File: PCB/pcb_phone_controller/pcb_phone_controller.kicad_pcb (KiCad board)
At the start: 2 copper layers, 115.3 x 53.2 mm, 39 parts, among them SW17 SS-12D00-G 4 E, X1 KAILH-MINI-SILENT-SWITCH, Y1 KAILH-MINI-SILENT-SWITCH

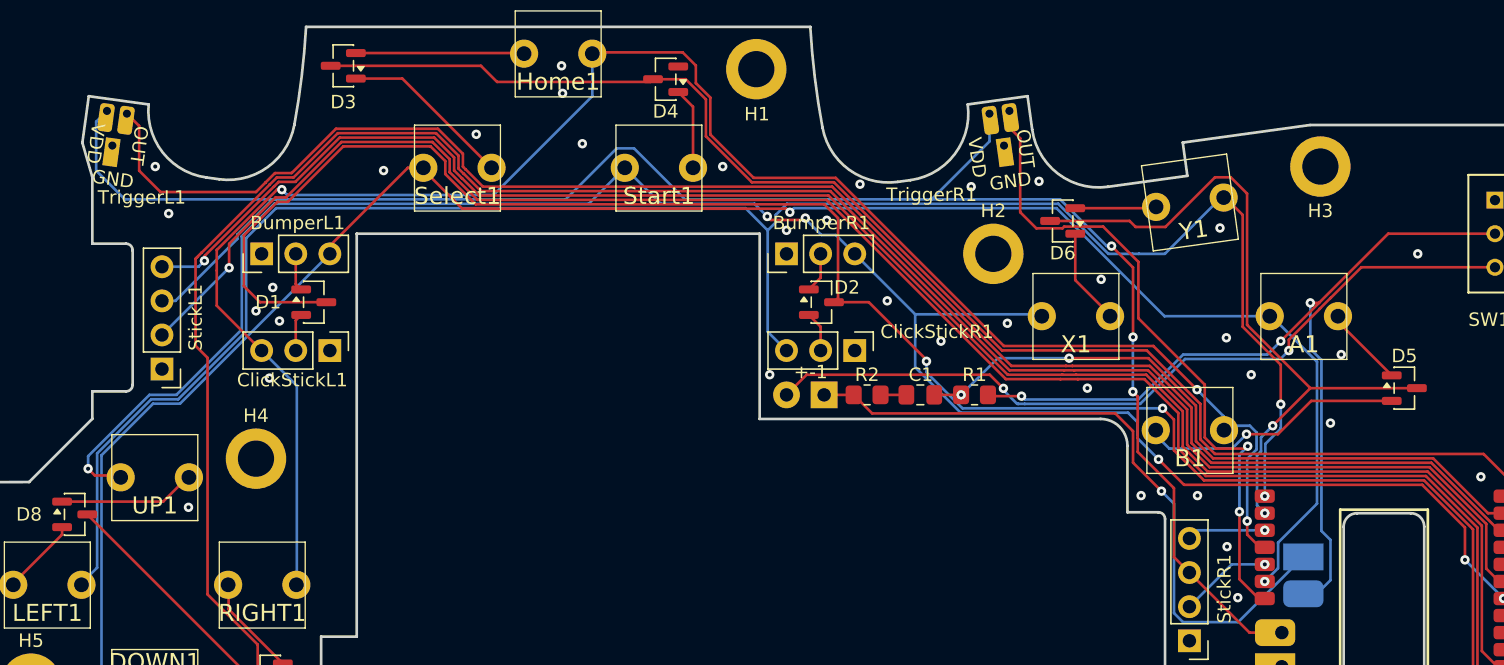
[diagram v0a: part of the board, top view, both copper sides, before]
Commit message: Change capacitives buttons to digitals ones and add real pullup
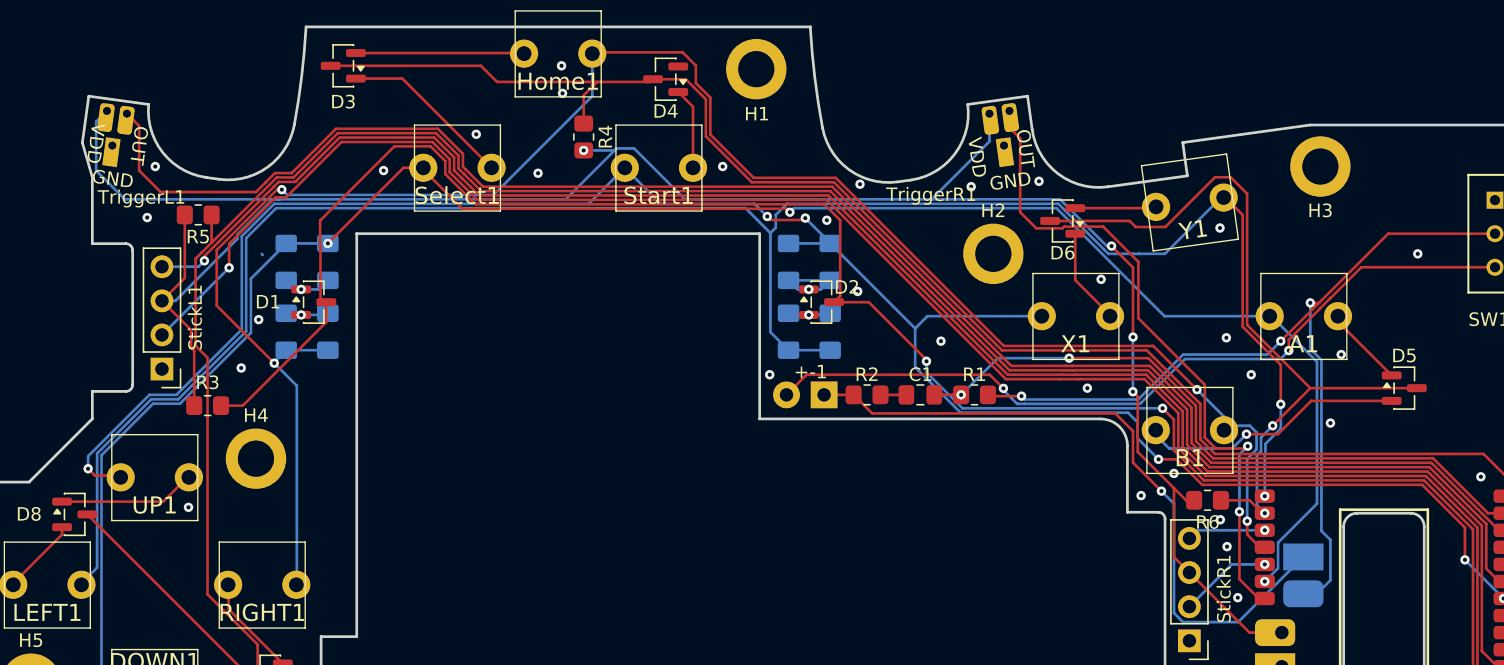
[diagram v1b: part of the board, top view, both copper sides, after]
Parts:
- added R3: 10k, Resistor_SMD:R_0805_2012Metric_Pad1.20x1.40mm_HandSolder, F.Cu at (123.9, 123.3)
- added R4: 10k, Resistor_SMD:R_0805_2012Metric_Pad1.20x1.40mm_HandSolder, F.Cu at (151.9, 103.3)
- added R5: 10k, Resistor_SMD:R_0805_2012Metric_Pad1.20x1.40mm_HandSolder, F.Cu at (123.2, 109.1)
- added R6: 10k, Resistor_SMD:R_0805_2012Metric_Pad1.20x1.40mm_HandSolder, F.Cu at (198.3, 130.3)
- BumperL1, BumperR1, ClickStickL1, ClickStickR1: value ~ -> Thin membrane button; footprint Lib_controller:TTP223 -> Lib_controller:SKRWADE030; moved to B.Cu
- moved ClickStickR1 3.66 mm to (168.7, 117.8), turned to 180 degrees
- moved BumperL1 3.43 mm to (131.3, 112.6), turned to 180 degrees
- moved ClickStickL1 2.20 mm to (131.3, 117.8), turned to 180 degrees
- moved BumperR1 1.80 mm to (168.7, 112.6), turned to 180 degrees
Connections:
- BumperL1 pad 1: GND -> Column 0
- BumperR1 pad 1: GND -> Column 2
- ClickStickL1 pad 1: GND -> Net-(ClickStickL1-Pad1)
- ClickStickL1 pad 2: Net-(ClickStickL1-I/O) -> Column 1
- ClickStickR1 pad 1: GND -> Net-(ClickStickR1-Pad1)
- ClickStickR1 pad 2: Net-(ClickStickR1-I/O) -> Column 3
- D1 pad 2: Net-(ClickStickL1-I/O) -> Net-(ClickStickL1-Pad1)
- D2 pad 2: Net-(ClickStickR1-I/O) -> Net-(ClickStickR1-Pad1)
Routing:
- net +3.3V: track 141.5 -> 161.8 mm, vias 3 -> 4
- net Column 1: track 137.4 -> 141.9 mm, vias 3 -> 4
- net Net-(BumperR1-Pad2): track 3.01 -> 6.76 mm, vias 0 -> 1
- net Row 2: track 52.5 -> 56.1 mm
- net Column 2: track 149.4 -> 153.1 mm
- net Row 1: track 114.9 -> 118.5 mm
- net Column 3: track 145.0 -> 148.2 mm
- net Net-(ClickStickR1-Pad1): track 0.00 -> 3.20 mm, vias 0 -> 1
- net Net-(ClickStickL1-Pad1): track 0.00 -> 3.20 mm, vias 0 -> 1
- net Net-(ClickStickR1-I/O): track 3.01 -> 0.00 mm
- net Net-(ClickStickL1-I/O): track 2.82 -> 0.00 mm
- net Column 0: track 142.2 -> 144.3 mm, vias 2 -> 3
- net Row 3: track 169.8 -> 171.9 mm
- net Row 0: track 144.4 -> 146.4 mm
- net Net-(BumperL1-Pad2): track 2.82 -> 3.66 mm, vias 0 -> 1
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
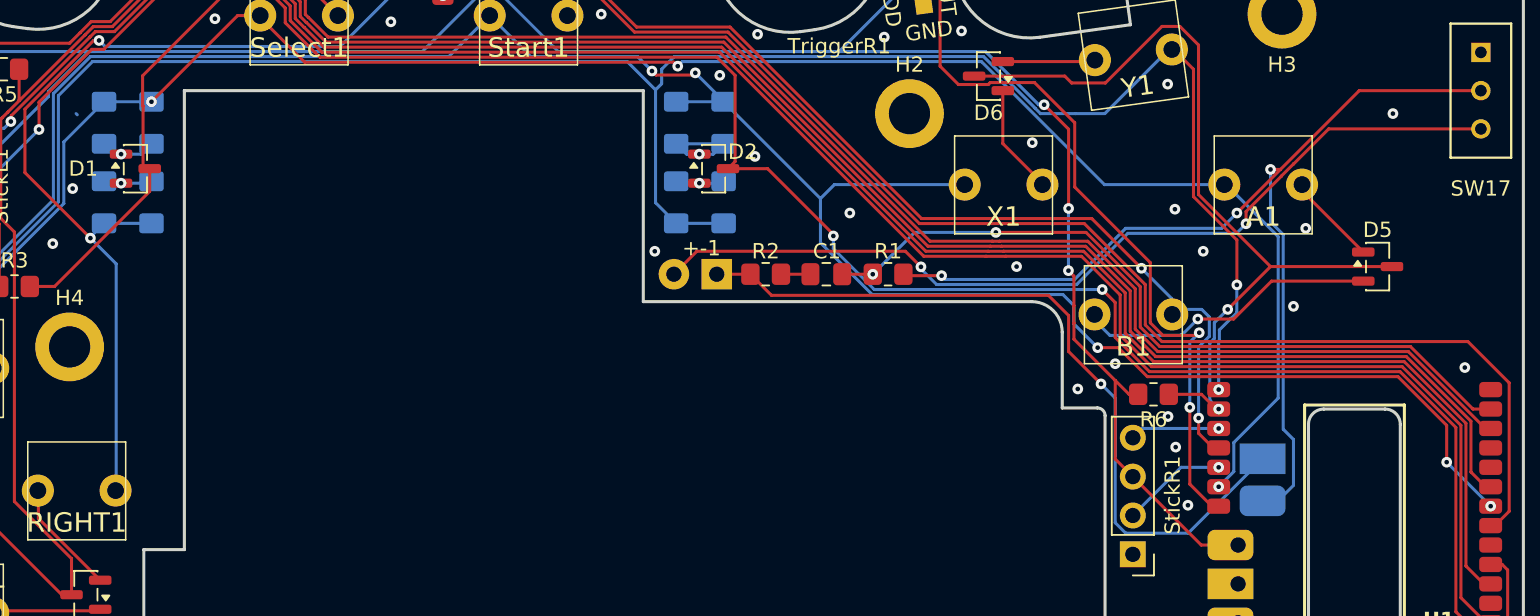
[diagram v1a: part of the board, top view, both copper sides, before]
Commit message: Add a 3D model for the back buttons
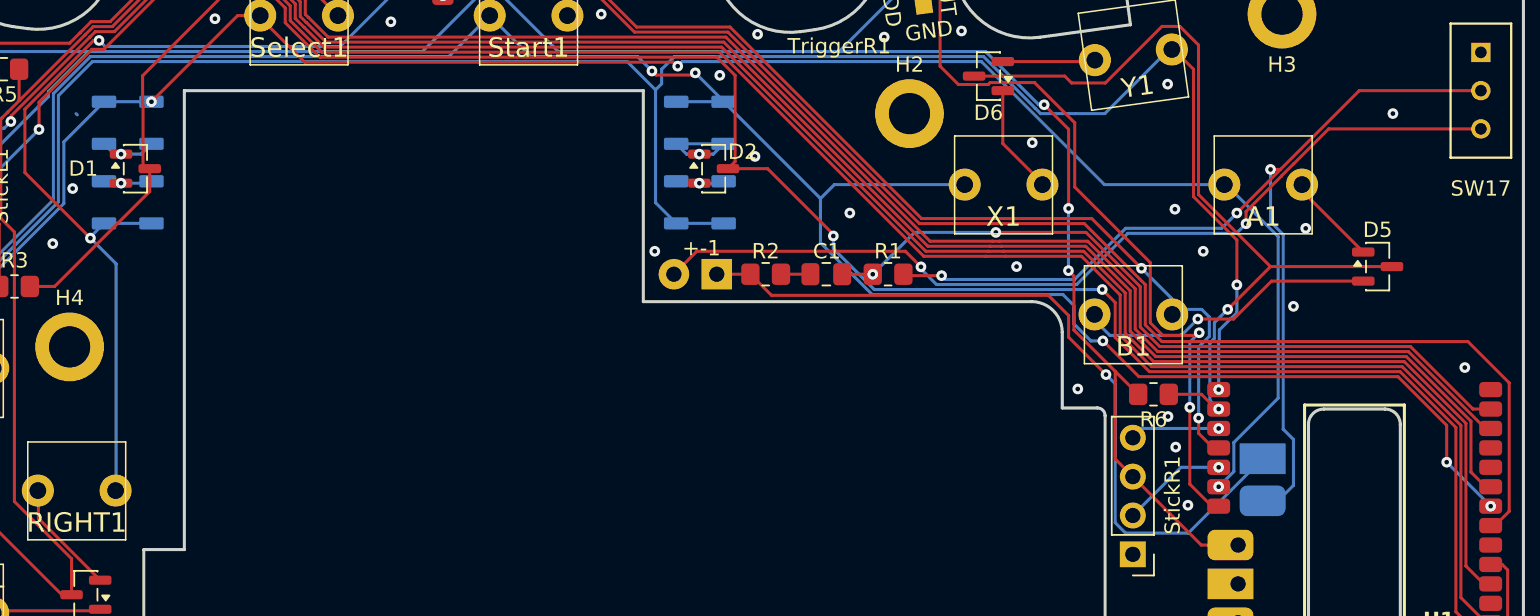
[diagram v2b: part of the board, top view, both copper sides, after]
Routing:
- net GND: vias 32 -> 31

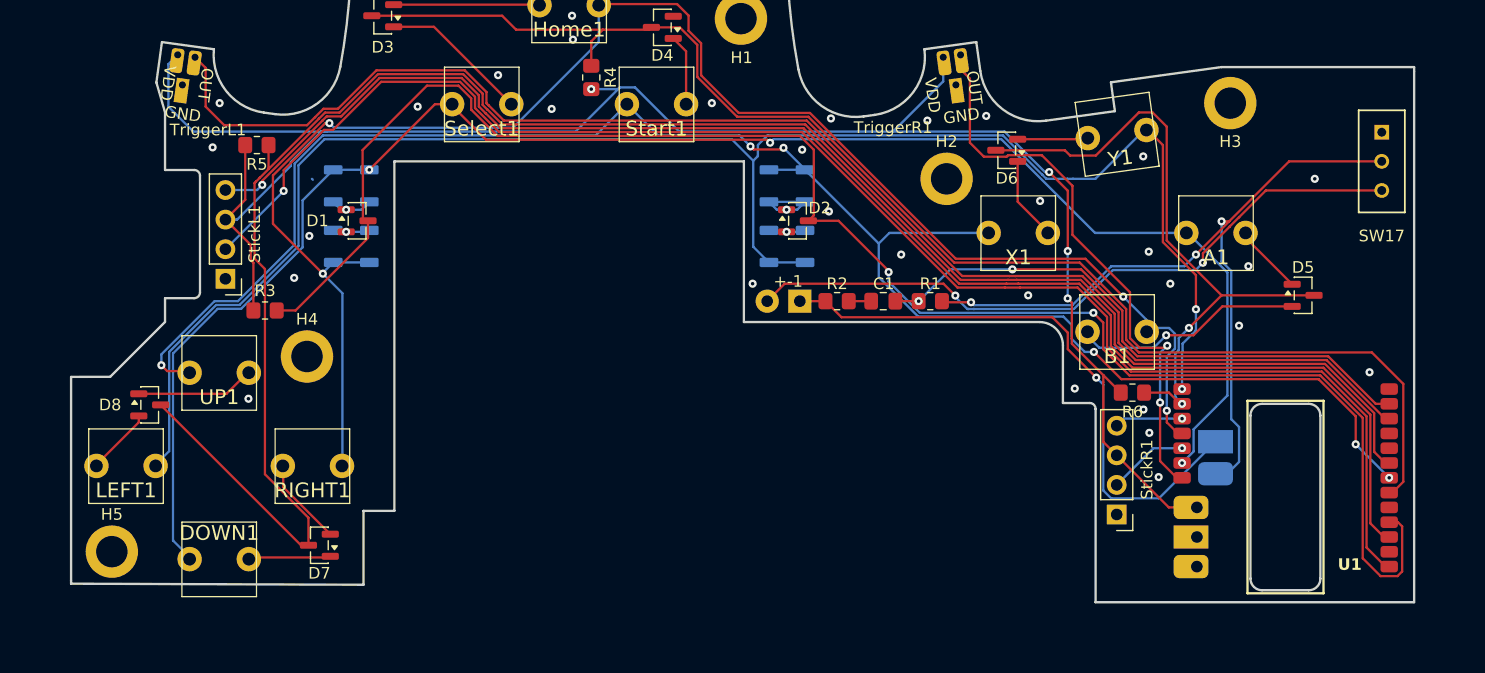
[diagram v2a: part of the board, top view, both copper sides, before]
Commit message: Add the PCB in the BOM and make the PCB smaller
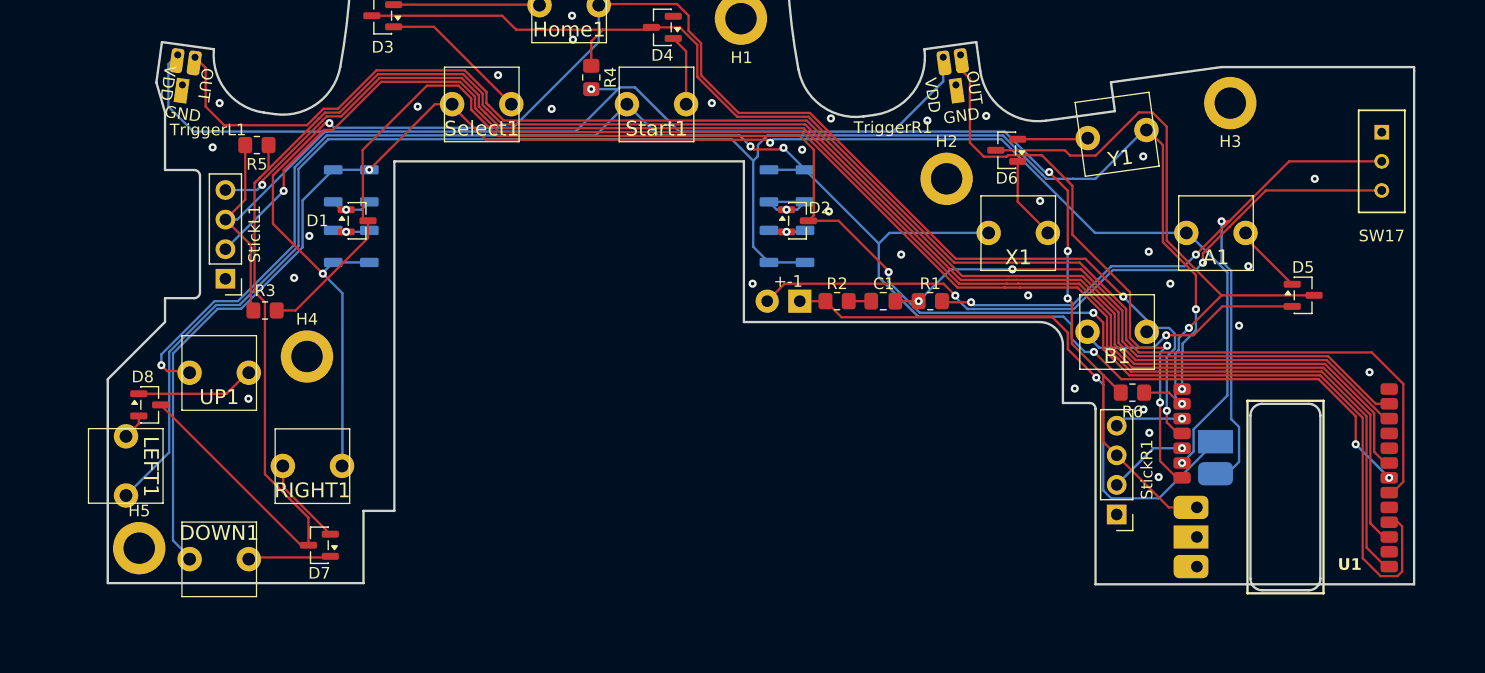
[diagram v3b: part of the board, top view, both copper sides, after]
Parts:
- moved H5 2.37 mm to (113.1, 143.7)
- turned LEFT1 to -90 degrees
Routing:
- net Column 3: track 148.2 -> 151.8 mm
- net Net-(D8-Pad2): track 5.64 -> 2.21 mm
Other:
- board size 115.3 x 53.2 mm -> 112.1 x 51.7 mm

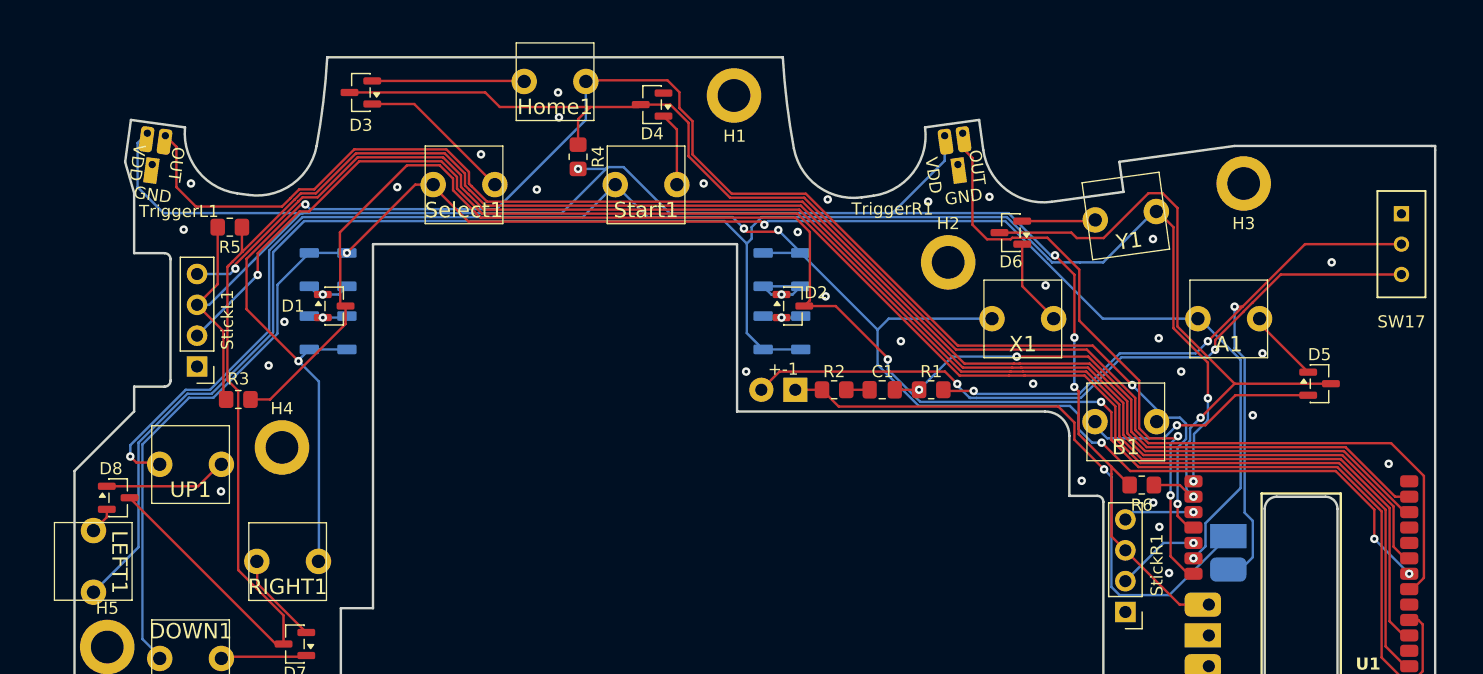
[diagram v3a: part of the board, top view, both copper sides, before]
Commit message: Reroute the PCB to move the buttons
Signed-off-by: LAPCoder <lapcoder.gh@gmail.com>
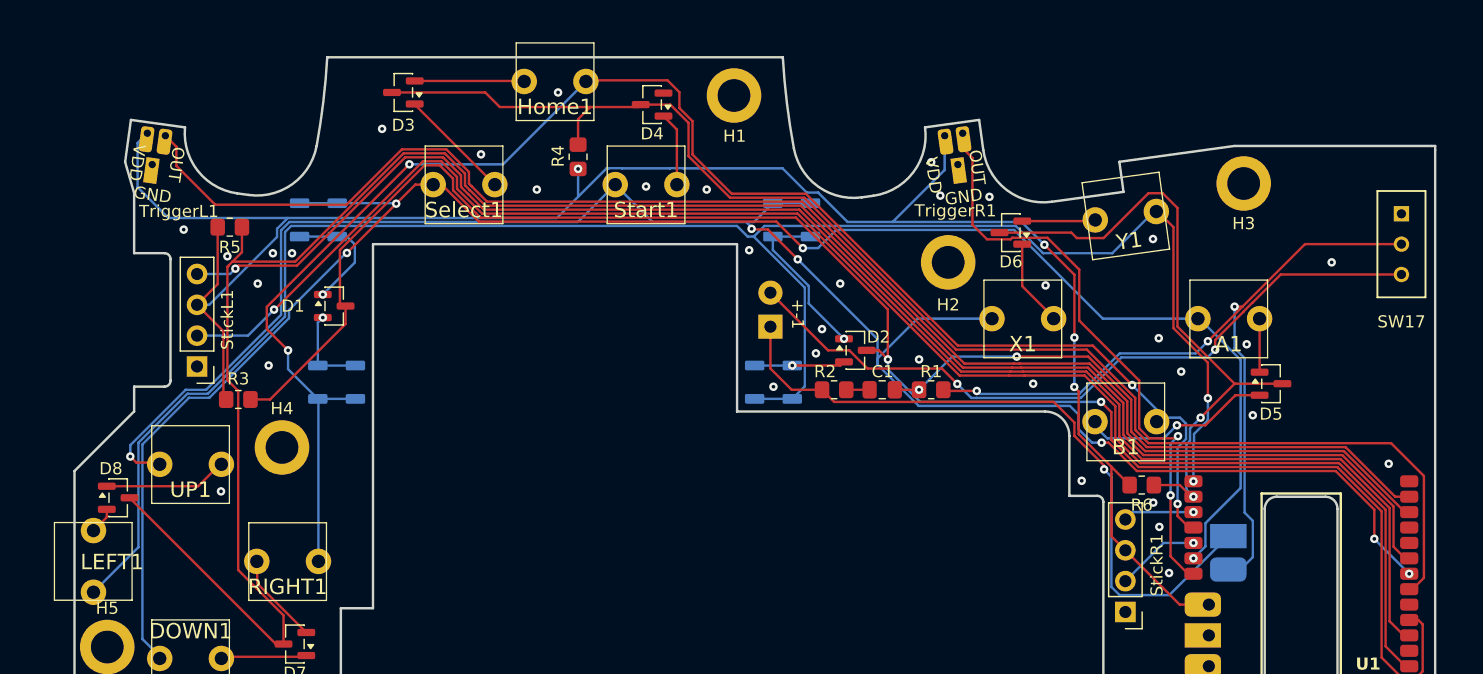
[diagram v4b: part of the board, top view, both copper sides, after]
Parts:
- moved +-1 7.78 mm to (166.8, 115.9), turned to 90 degrees
- moved D2 6.31 mm to (174.8, 119.2)
- moved BumperL1 4.18 mm to (130.5, 108.5)
- moved BumperR1 4.18 mm to (169.5, 108.5)
- moved ClickStickL1 4.13 mm to (132.0, 121.9)
- moved ClickStickR1 4.13 mm to (168.0, 121.9)
- moved D5 4.00 mm to (209.0, 122.0)
- moved D3 3.50 mm to (137.5, 98.0)
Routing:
- net Column 1: track 141.9 -> 133.7 mm
- net Net-(BumperR1-Pad2): track 6.76 -> 14.0 mm
- net Column 0: track 144.3 -> 151.1 mm, vias 3 -> 4
- net Net-(BumperL1-Pad2): track 3.66 -> 10.0 mm
- net -BATT: track 50.9 -> 57.1 mm
- net Net-(ClickStickR1-Pad1): track 3.20 -> 7.49 mm
- net Net-(ClickStickL1-Pad1): track 3.20 -> 7.22 mm
- net Net-(B1-Pad1): track 20.0 -> 16.0 mm
- net Row 2: track 56.1 -> 52.1 mm
- net Column 3: track 151.8 -> 155.6 mm
- net Column 2: track 152.9 -> 156.6 mm
- net Row 1: track 118.5 -> 115.0 mm
- net Net-(D3-Pad1): track 12.8 -> 9.36 mm
- net Net-(D3-Pad2): track 12.5 -> 9.11 mm
- net Net-(A1-Pad2): track 6.22 -> 4.94 mm
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
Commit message: Modify a bit the PCB
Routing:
- net Column 2: track 156.6 -> 158.4 mm
- net +BATT: track 67.4 -> 66.7 mm
- net GND: vias 35 -> 34
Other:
- outline, holes or cut-outs redrawn
